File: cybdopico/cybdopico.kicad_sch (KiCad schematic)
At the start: 0 parts

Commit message: journal 1
its 11pm but i wanted to get started anyway
im gonna try and speedrun this all tomorrow since i dont really have much time after that.

this is my 3rd time designing a rp2040 minimum system so it should be good...

anyways laid out the footprint and mcu and connected gpio
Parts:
- added A1: RaspberryPi_Pico, Module:RaspberryPi_Pico_Common_Unspecified, symbol MCU_Module:RaspberryPi_Pico
- added U1: RP2040, Package_DFN_QFN:QFN-56-1EP_7x7mm_P0.4mm_EP3.2x3.2mm, symbol MCU_RaspberryPi:RP2040
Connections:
- new net: U1.1 (IOVDD), U1.10 (IOVDD), U1.22 (IOVDD), U1.33 (IOVDD), U1.42 (IOVDD), U1.49 (IOVDD)
- new net: U1.23 (DVDD), U1.50 (DVDD)
- new net GND: A1.13 (GND), A1.18 (GND), A1.23 (GND), A1.28 (GND), A1.3 (GND), A1.33 (AGND), A1.38 (GND), A1.8 (GND), U1.57 (GND)
- new net GPIO0: A1.1 (GPIO0), U1.2 (GPIO0)
- new net GPIO1: A1.2 (GPIO1), U1.3 (GPIO1)
- new net GPIO10: A1.14 (GPIO10), U1.13 (GPIO10)
- new net GPIO11: A1.15 (GPIO11), U1.14 (GPIO11)
- new net GPIO12: A1.16 (GPIO12), U1.15 (GPIO12)
- new net GPIO13: A1.17 (GPIO13), U1.16 (GPIO13)
- new net GPIO14: A1.19 (GPIO14), U1.17 (GPIO14)
- new net GPIO15: A1.20 (GPIO15), U1.18 (GPIO15)
- new net GPIO16: A1.21 (GPIO16), U1.27 (GPIO16)
- new net GPIO17: A1.22 (GPIO17), U1.28 (GPIO17)
- new net GPIO18: A1.24 (GPIO18), U1.29 (GPIO18)
- new net GPIO19: A1.25 (GPIO19), U1.30 (GPIO19)
- new net GPIO2: A1.4 (GPIO2), U1.4 (GPIO2)
- new net GPIO20: A1.26 (GPIO20), U1.31 (GPIO20)
- new net GPIO21: A1.27 (GPIO21), U1.32 (GPIO21)
- new net GPIO22: A1.29 (GPIO22), U1.34 (GPIO22)
- new net GPIO23: U1.35 (GPIO23)
- new net GPIO24: U1.36 (GPIO24)
- new net GPIO25: U1.37 (GPIO25)
- new net GPIO26: A1.31 (GPIO26_ADC0), U1.38 (GPIO26_ADC0)
- new net GPIO27: A1.32 (GPIO27_ADC1), U1.39 (GPIO27_ADC1)
- new net GPIO28: A1.34 (GPIO28_ADC2), U1.40 (GPIO28_ADC2)
- new net GPIO29: U1.41 (GPIO29_ADC3)
- new net GPIO3: A1.5 (GPIO3), U1.5 (GPIO3)
- new net GPIO4: A1.6 (GPIO4), U1.6 (GPIO4)
- new net GPIO5: A1.7 (GPIO5), U1.7 (GPIO5)
- new net GPIO6: A1.9 (GPIO6), U1.8 (GPIO6)
- new net GPIO7: A1.10 (GPIO7), U1.9 (GPIO7)
- new net GPIO8: A1.11 (GPIO8), U1.11 (GPIO8)
- new net GPIO9: A1.12 (GPIO9), U1.12 (GPIO9)

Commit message: finished everything
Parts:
- added C1, C2: 10uF, Capacitor_SMD:C_0603_1608Metric_Pad1.08x0.95mm_HandSolder, symbol Device:C
- added C10, C11, C12, C14, C15, C6, C7, C8, C9: 100nF, Capacitor_SMD:C_0603_1608Metric_Pad1.08x0.95mm_HandSolder, symbol Device:C
- added C13, C5: 1uF, Capacitor_SMD:C_0603_1608Metric_Pad1.08x0.95mm_HandSolder, symbol Device:C
- added C3, C4: 15pF, Capacitor_SMD:C_0603_1608Metric_Pad1.08x0.95mm_HandSolder, symbol Device:C
- added D1: 1N5819WS, Diode_SMD:D_SOD-323, symbol Diode:1N5819WS
- added P1: USB_C_Plug_USB2.0, imports:TYPE-C-31-M-12, symbol Connector:USB_C_Receptacle_USB2.0_14P
- added R1, R2, R5: 27R, Resistor_SMD:R_0603_1608Metric_Pad0.98x0.95mm_HandSolder, symbol Device:R
- added R14, R8: 1kR, Resistor_SMD:R_0603_1608Metric, symbol Device:R
- added R3, R4: 5k1R, Resistor_SMD:R_0603_1608Metric_Pad0.98x0.95mm_HandSolder, symbol Device:R
- added R6: 1kR, Resistor_SMD:R_0603_1608Metric_Pad0.98x0.95mm_HandSolder, symbol Device:R
- added R7: 1MR, Resistor_SMD:R_0603_1608Metric, symbol Device:R
- added SW1: BOOTSEL, Button_Switch_SMD:SW_Push_SPST_NO_Alps_SKRK, symbol Switch:SW_Push
- added SW2: RESET, Button_Switch_SMD:SW_Push_SPST_NO_Alps_SKRK, symbol Switch:SW_Push
- added SW3: HC FLAG, Library:hackclub flag touch, symbol Switch:SW_Push
- added U2: USBLC6-2SC6, Package_TO_SOT_SMD:SOT-23-6, symbol Power_Protection:USBLC6-2SC6
- added U3: W25Q16JVUXIQ, Package_SON:Winbond_USON-8-1EP_3x2mm_P0.5mm_EP0.2x1.6mm, symbol Memory_Flash:W25Q128JVP
- added U4: MCP1700x-330xxTT, Package_TO_SOT_SMD:SOT-23, symbol Regulator_Linear:MCP1700x-330xxTT
- added Y1: ABM8-272-T3, Crystal:Crystal_SMD_Abracon_ABM8G-4Pin_3.2x2.5mm, symbol ABM8-272-T3:ABM8-272-T3
- A1: now not fitted; now left out of the parts list
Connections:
- net GND: now also U1.19 (TESTEN), C1.2, C10.2, C11.2, C12.2, C13.2, C14.2, C15.2, C2.2, C3.2, C4.2, C5.2, C6.2, C7.2, C8.2, C9.2, P1.A1 (GND), P1.A12 (GND), P1.B1 (GND), P1.B12 (GND), P1.Sh1 (SHIELD), R3.2, R4.2, R6.1, R8.2, SW2.1, U2.2 (GND), U3.4 (GND), U3.9 (EP), U4.1 (GND), Y1.2 (GND), Y1.4 (GND)
- net GPIO29: now also A1.37 (3V3_EN)
- net RUN: now reaches A1.30 (RUN)
- net RUN: now also U1.26 (RUN), SW2.2
- net +3V3: now reaches A1.35 (ADC_VREF)
- net +3V3: now also A1.36 (3V3), U1.1 (IOVDD), U1.10 (IOVDD), U1.22 (IOVDD), U1.33 (IOVDD), U1.42 (IOVDD), U1.43 (ADC_AVDD), U1.44 (VREG_IN), U1.48 (USB_VDD), U1.49 (IOVDD), C10.1, C11.1, C12.1, C2.1, C5.1, C6.1, C7.1, C8.1, C9.1, R5.2, R7.1, U3.8 (VCC), U4.2 (VO)
- net VSYS: now reaches A1.39 (VSYS)
- net VSYS: now also C1.1, D1.1 (K), U4.3 (VI)
- net VBUS: now reaches A1.40 (VBUS)
- net VBUS: now also D1.2 (A), P1.A4 (VBUS), P1.A9 (VBUS), P1.B4 (VBUS), P1.B9 (VBUS), U2.5 (VBUS)
- net XIN: now reaches U1.20 (XIN)
- net XIN: now also C4.1, Y1.1
- net XOUT: now reaches U1.21 (XOUT)
- net XOUT: now also R14.2
- net +1V1: now reaches U1.23 (DVDD), U1.50 (DVDD)
- net +1V1: now also U1.45 (VREG_VOUT), C13.1, C14.1, C15.1
- net at U1.46 (USB_DM): now also R2.2
- net at U1.47 (USB_DP): now also R1.2
- net FLASH_SD3: now reaches U1.51 (QSPI_SD3)
- net FLASH_SD3: now also U3.7 (~{HOLD}/~{RESET}/IO_{3})
- net FLASH_SCLK: now reaches U1.52 (QSPI_SCLK)
- net FLASH_SCLK: now also U3.6 (CLK)
- net FLASH_SD0: now reaches U1.53 (QSPI_SD0)
- net FLASH_SD0: now also U3.5 (DI/IO_{0})
- net FLASH_SD2: now reaches U1.54 (QSPI_SD2)
- net FLASH_SD2: now also U3.3 (~{WP}/IO_{2})
- net FLASH_SD1: now reaches U1.55 (QSPI_SD1)
- net FLASH_SD1: now also U3.2 (DO/IO_{1})
- net FLASH_SS: now reaches U1.56 (QSPI_SS)
- net FLASH_SS: now also R5.1, SW1.2, U3.1 (~{CS})
- net GPIO23: no longer names the net of U1.35 (GPIO23)
- net GPIO24 renamed GPIO24-TOUCH-BTN
- net GPIO24-TOUCH-BTN: now also R7.2, SW3.2
- net GPIO25: no longer names the net of U1.37 (GPIO25)
- new net: R6.2, SW1.1
- new net: R8.1, SW3.1
- new net: P1.B5 (CC2), R4.1
- new net: C3.1, R14.1, Y1.3
- new net: P1.A5 (CC1), R3.1
- new net: P1.A7 (D-), P1.B7 (D-), U2.1 (I/O1)
- new net: P1.A6 (D+), P1.B6 (D+), U2.3 (I/O2)
- new net USB_DM: R2.1, U2.6 (I/O1)
- new net USB_DP: R1.1, U2.4 (I/O2)
- no-connect marks 0 -> 4
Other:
- note added: "c13 next to 45, c14, c15 next to 23, 50"
- note added: "c5 next to 44, c6-12 next to 1, 10, 22, 33, (42,43), (48,49)"

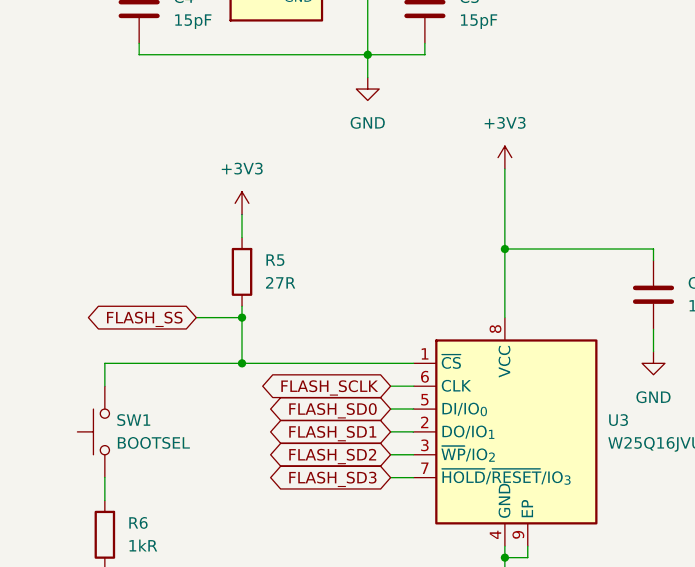
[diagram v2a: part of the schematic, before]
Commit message: fixed resistors and clearned up board (extra vias, traces, etc)
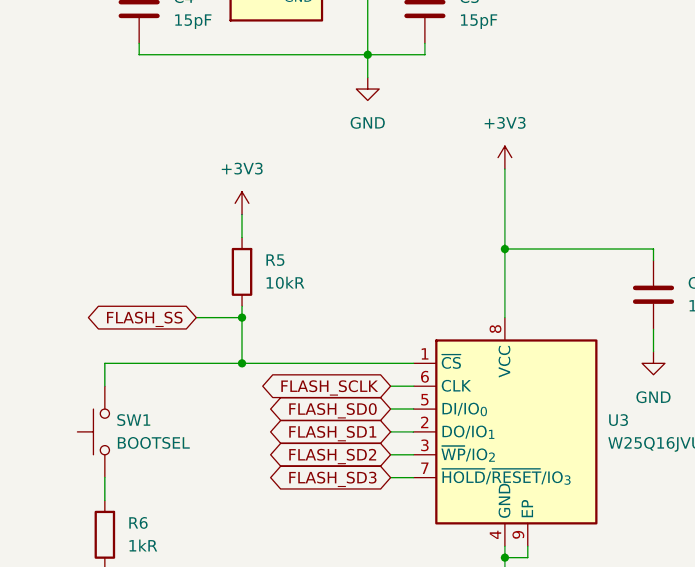
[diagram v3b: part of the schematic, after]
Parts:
- R5: value 27R -> 10kR
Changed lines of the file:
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@@
 			)
 		)
-		(property "Value" "27R"
+		(property "Value" "10kR"
 			(at 44.45 156.2099 0)
 			(effects
